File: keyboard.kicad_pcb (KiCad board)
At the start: 2 copper layers, 10 parts, among them U1 STM32F072CBT6

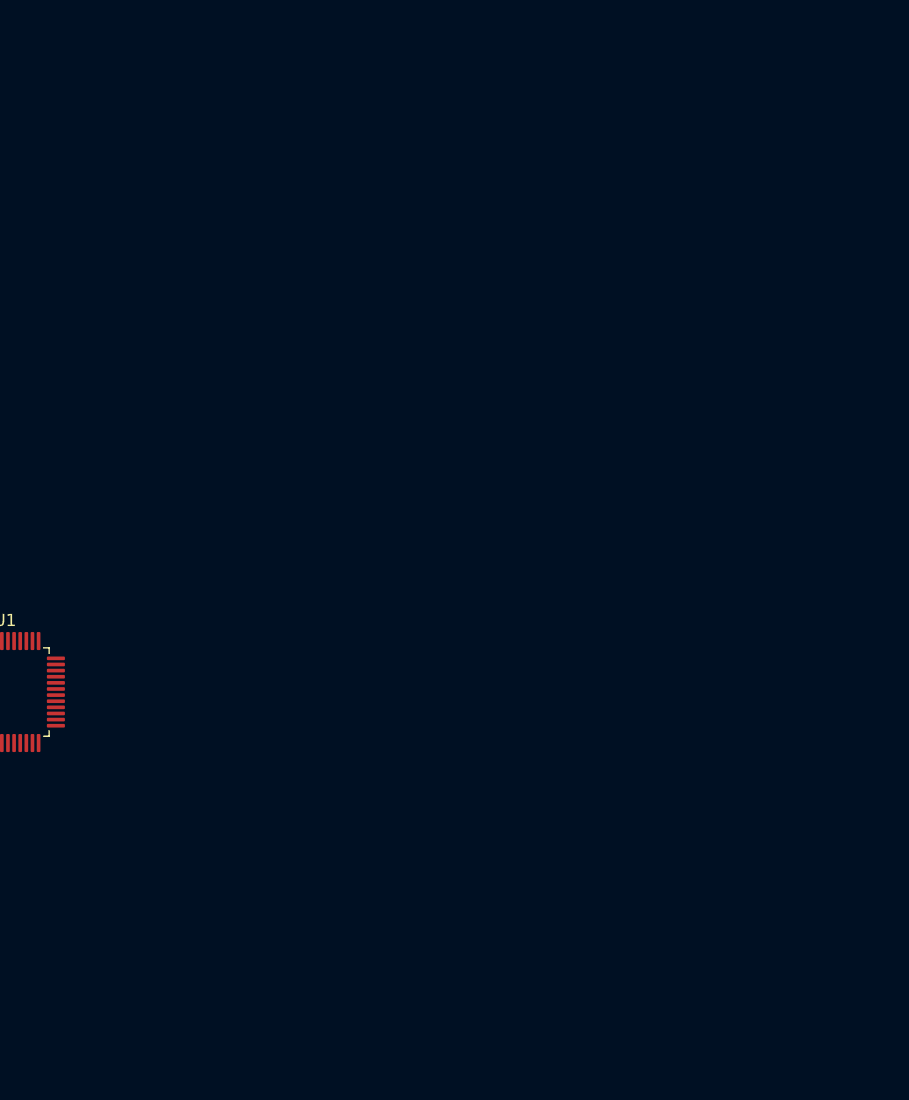
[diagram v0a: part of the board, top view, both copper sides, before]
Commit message: Added lcd display
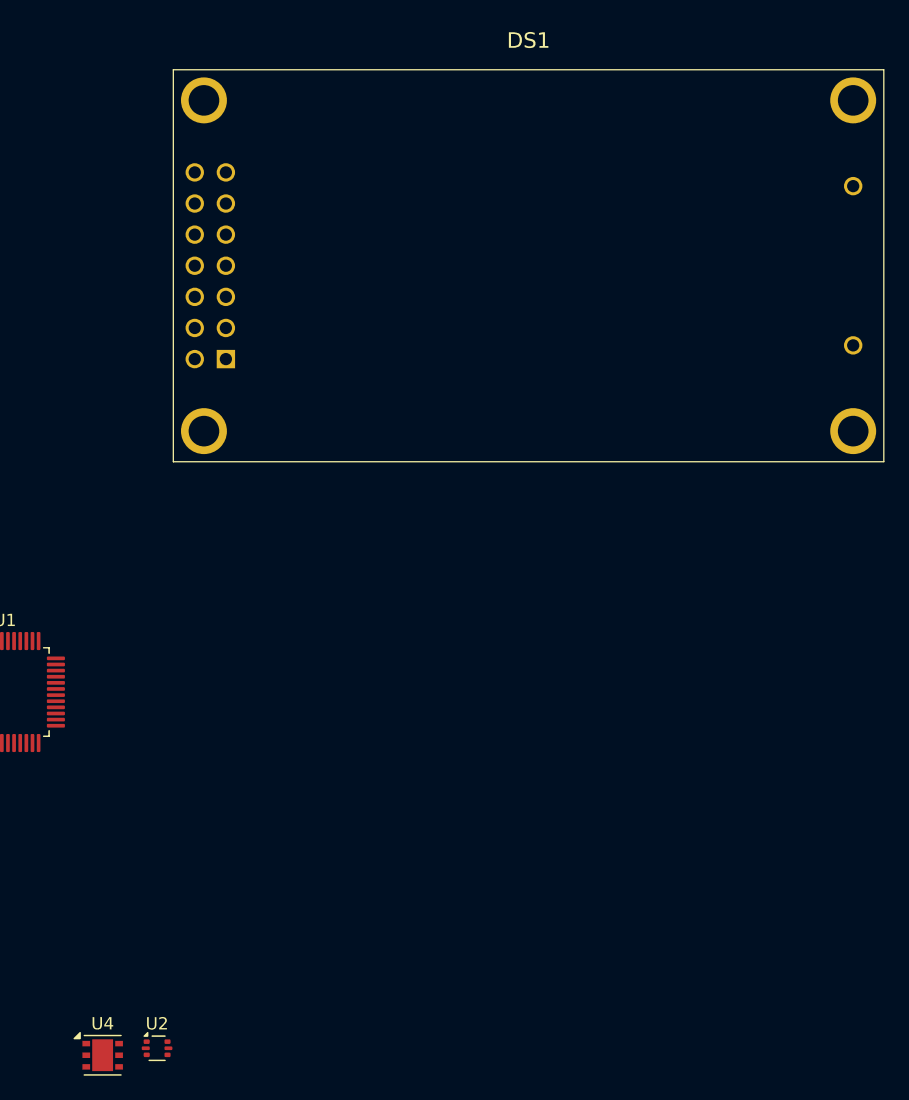
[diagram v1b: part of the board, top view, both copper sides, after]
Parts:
- added DS1: NHD-0208BZ-FL-YBW, NHD:NHD0208BZFLYBW, F.Cu at (118.8, 45.7)
- added U2: USBLC6-2P6, Package_TO_SOT_SMD:SOT-666, F.Cu at (113.2, 102.0)
- added U4: LDO40LPU33RY, Package_DFN_QFN:DFN-6-1EP_3x3mm_P0.95mm_EP1.7x2.6mm, F.Cu at (108.8, 102.5)
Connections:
- U1 pad 21: unconnected-(U1-PB10-Pad21) -> /LCD_ENABLE
- U1 pad 22: unconnected-(U1-PB11-Pad22) -> /DB4
- U1 pad 25: unconnected-(U1-PB12-Pad25) -> /DB5
- U1 pad 26: unconnected-(U1-PB13-Pad26) -> /DB6
- U1 pad 27: unconnected-(U1-PB14-Pad27) -> /DB7
- U1 pad 40: unconnected-(U1-PB4-Pad40) -> /OUT_A
- U1 pad 41: unconnected-(U1-PB5-Pad41) -> /OUT_B
- U1 pad 43: unconnected-(U1-PB7-Pad43) -> /MUTE
- U1 pad 45: unconnected-(U1-PB8-Pad45) -> /LED
- U1 pad 46: unconnected-(U1-PB9-Pad46) -> /LCD_RS

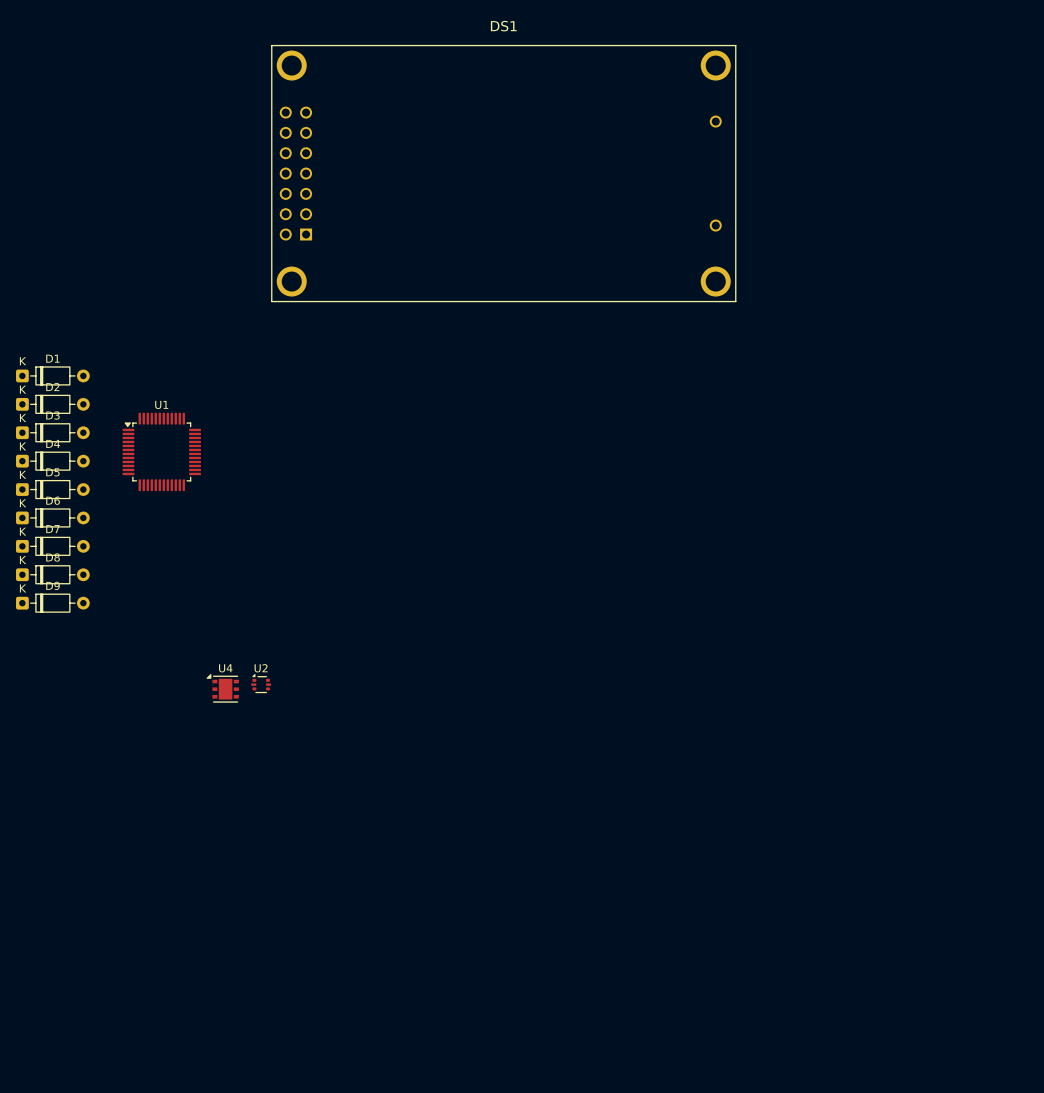
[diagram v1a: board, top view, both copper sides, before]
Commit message: Added key switches footprints
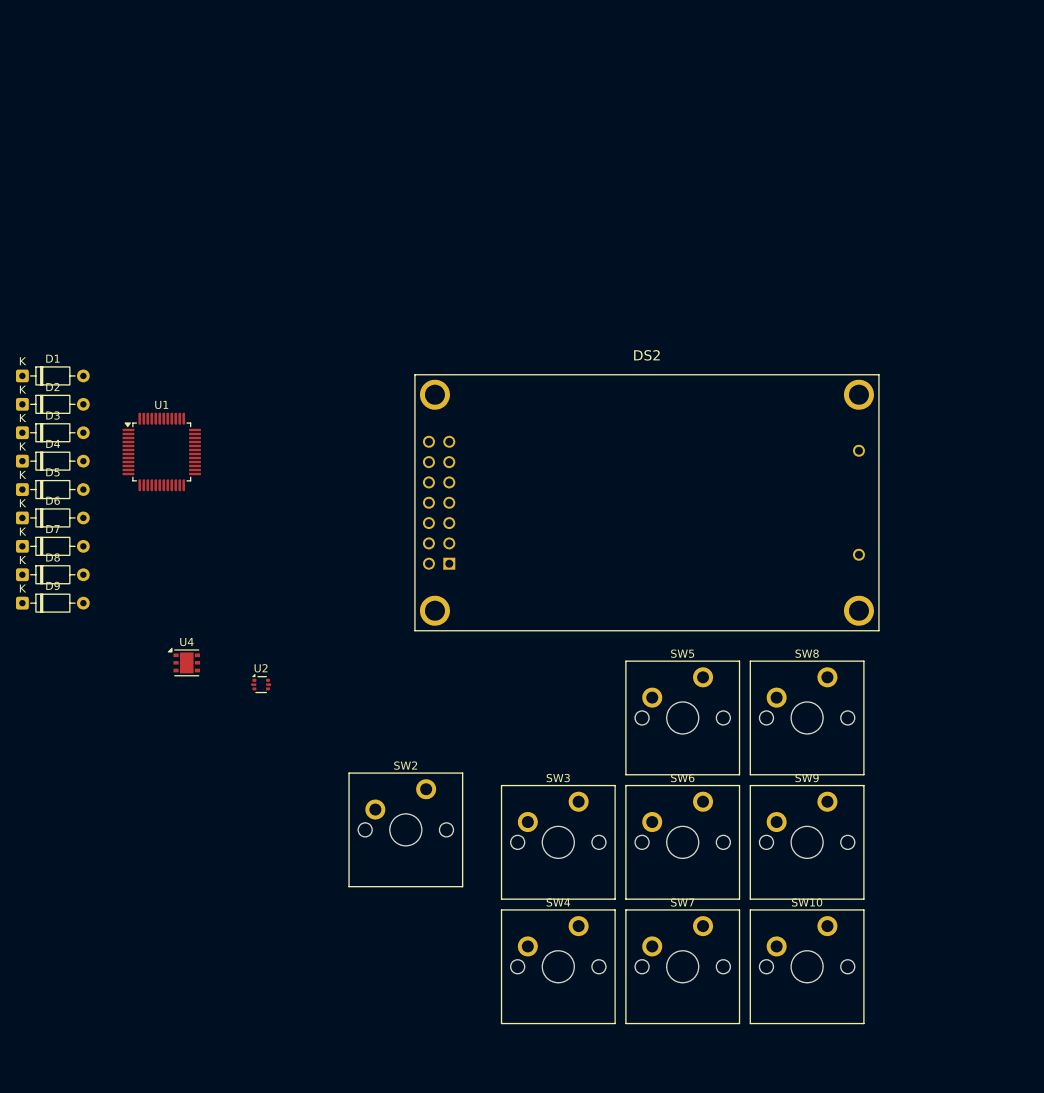
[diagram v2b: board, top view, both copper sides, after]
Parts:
- removed DS1: NHD-0208BZ-FL-YBW, NHD:NHD0208BZFLYBW
- added DS2: NHD-0208BZ-FL-YBW, NHD:NHD0208BZFLYBW, F.Cu at (136.7, 86.9)
- added SW10: SW_Push, Switch_Keyboard_Cherry_MX:SW_Cherry_MX_PCB_1.00u, F.Cu at (181.5, 137.2)
- added SW2: SW_Push, Switch_Keyboard_Cherry_MX:SW_Cherry_MX_PCB_1.00u, F.Cu at (131.3, 120.1)
- added SW3: SW_Push, Switch_Keyboard_Cherry_MX:SW_Cherry_MX_PCB_1.00u, F.Cu at (150.4, 121.7)
- added SW4: SW_Push, Switch_Keyboard_Cherry_MX:SW_Cherry_MX_PCB_1.00u, F.Cu at (150.4, 137.2)
- added SW5: SW_Push, Switch_Keyboard_Cherry_MX:SW_Cherry_MX_PCB_1.00u, F.Cu at (165.9, 106.2)
- added SW6: SW_Push, Switch_Keyboard_Cherry_MX:SW_Cherry_MX_PCB_1.00u, F.Cu at (165.9, 121.7)
- added SW7: SW_Push, Switch_Keyboard_Cherry_MX:SW_Cherry_MX_PCB_1.00u, F.Cu at (165.9, 137.2)
- added SW8: SW_Push, Switch_Keyboard_Cherry_MX:SW_Cherry_MX_PCB_1.00u, F.Cu at (181.5, 106.2)
- added SW9: SW_Push, Switch_Keyboard_Cherry_MX:SW_Cherry_MX_PCB_1.00u, F.Cu at (181.5, 121.7)
- moved U4 5.86 mm to (103.9, 99.3)

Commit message: Added footprints and placement
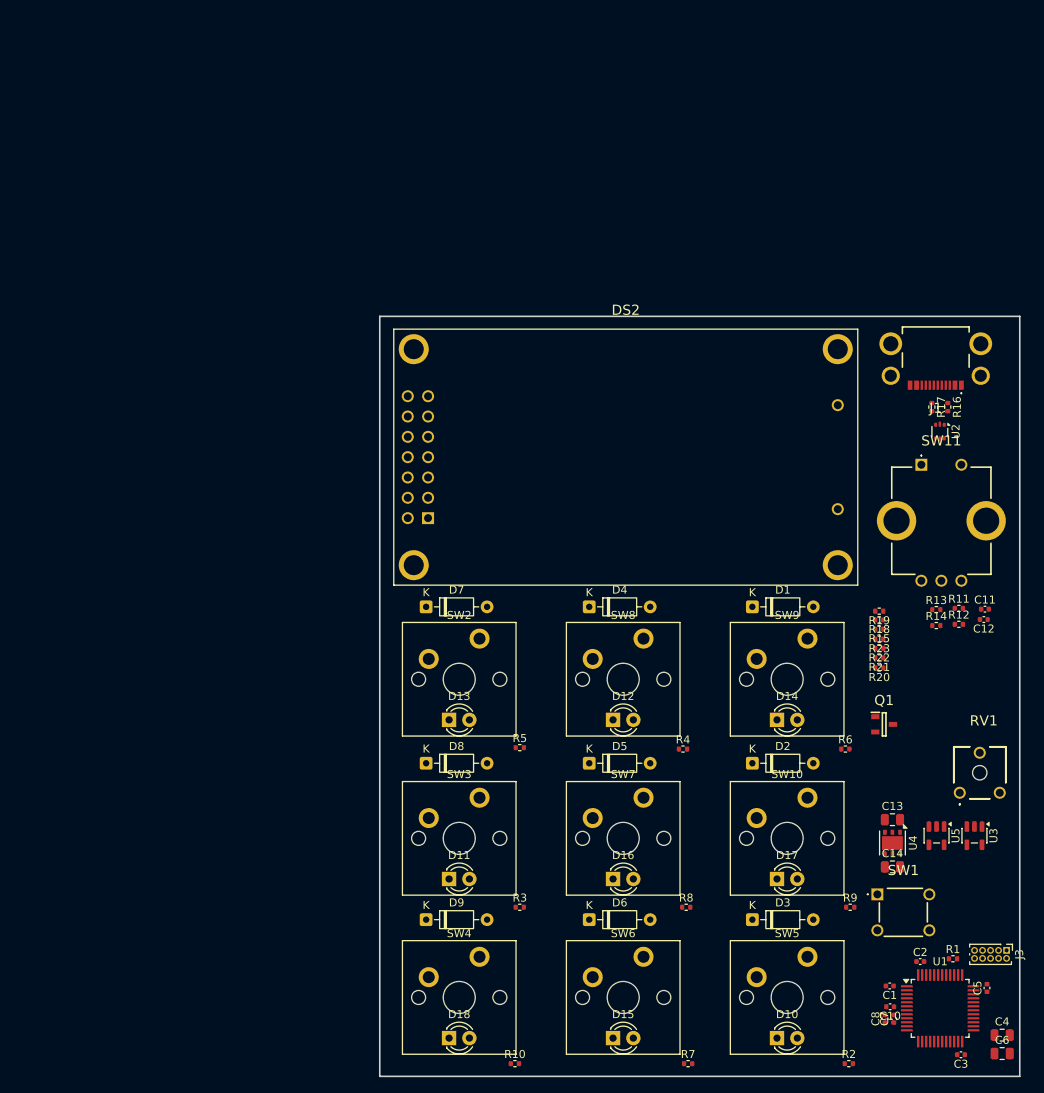
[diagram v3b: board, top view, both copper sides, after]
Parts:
- added C1: 100n, Capacitor_SMD:C_0402_1005Metric, F.Cu at (191.8, 139.7)
- added C10: 100n, Capacitor_SMD:C_0402_1005Metric, F.Cu at (191.8, 142.2)
- added C11: 100n, Capacitor_SMD:C_0402_1005Metric, F.Cu at (203.7, 92.5)
- added C12: 100n, Capacitor_SMD:C_0402_1005Metric, F.Cu at (203.6, 93.8)
- added C13: 4.7u, Capacitor_SMD:C_0805_2012Metric, F.Cu at (192.1, 118.9)
- added C14: 4.7u, Capacitor_SMD:C_0805_2012Metric, F.Cu at (192.1, 124.8)
- added C2: 100n, Capacitor_SMD:C_0402_1005Metric, F.Cu at (195.6, 136.6)
- added C3: 100n, Capacitor_SMD:C_0402_1005Metric, F.Cu at (200.7, 148.2)
- added C4: 4.7u, Capacitor_SMD:C_0805_2012Metric, F.Cu at (205.8, 145.8)
- added C5: 100n, Capacitor_SMD:C_0402_1005Metric, F.Cu at (203.9, 139.9)
- added C6: 4.7u, Capacitor_SMD:C_0805_2012Metric, F.Cu at (205.8, 148.1)
- added C7: 100n, Capacitor_SMD:C_0402_1005Metric, F.Cu at (192.3, 143.8)
- added C8: 1u, Capacitor_SMD:C_0402_1005Metric, F.Cu at (191.2, 143.8)
- added D10: LED, LED_THT:LED_D3.0mm, F.Cu at (177.7, 146.2)
- added D11: LED, LED_THT:LED_D3.0mm, F.Cu at (136.7, 126.3)
- added D12: LED, LED_THT:LED_D3.0mm, F.Cu at (157.2, 106.4)
- added D13: LED, LED_THT:LED_D3.0mm, F.Cu at (136.7, 106.4)
- added D14: LED, LED_THT:LED_D3.0mm, F.Cu at (177.7, 106.4)
- added D15: LED, LED_THT:LED_D3.0mm, F.Cu at (157.2, 146.2)
- added D16: LED, LED_THT:LED_D3.0mm, F.Cu at (157.2, 126.3)
- added D17: LED, LED_THT:LED_D3.0mm, F.Cu at (177.7, 126.3)
- added D18: LED, LED_THT:LED_D3.0mm, F.Cu at (136.7, 146.2)
- added J1: USB_C_Receptacle_USB2.0_16P, my_footprints:UJ20CHGMSMT4BP16TR, F.Cu at (197.6, 60.9)
- added J3: Conn_01x10_Pin, Connector_PinHeader_1.00mm:PinHeader_2x05_P1.00mm_Vertical, F.Cu at (206.4, 135.2)
- added Q1: NMOS, my_footprints:SOT95P230X110-3N, F.Cu at (191.1, 107.0)
- added R1: 10k, Resistor_SMD:R_0402_1005Metric, F.Cu at (199.7, 136.2)
- added R10: 330R, Resistor_SMD:R_0402_1005Metric, F.Cu at (144.9, 149.4)
- added R11: 10k, Resistor_SMD:R_0402_1005Metric, F.Cu at (200.4, 92.5)
- added R12: 10k, Resistor_SMD:R_0402_1005Metric, F.Cu at (200.4, 94.4)
- added R13: 10k, Resistor_SMD:R_0402_1005Metric, F.Cu at (197.6, 92.6)
- added R14: 10k, Resistor_SMD:R_0402_1005Metric, F.Cu at (197.6, 94.6)
- added R15: 330R, Resistor_SMD:R_0402_1005Metric, F.Cu at (190.5, 95.0)
- added R16: 5k1, Resistor_SMD:R_0402_1005Metric, F.Cu at (199.1, 67.3)
- added R17: 5k1, Resistor_SMD:R_0402_1005Metric, F.Cu at (197.1, 67.3)
- added R18: 330R, Resistor_SMD:R_0402_1005Metric, F.Cu at (190.5, 93.9)
- added R19: 330R, Resistor_SMD:R_0402_1005Metric, F.Cu at (190.5, 92.8)
- added R2: 330R, Resistor_SMD:R_0402_1005Metric, F.Cu at (186.7, 149.4)
- added R20: 330R, Resistor_SMD:R_0402_1005Metric, F.Cu at (190.5, 99.9)
- added R21: 330R, Resistor_SMD:R_0402_1005Metric, F.Cu at (190.5, 98.6)
- added R22: 330R, Resistor_SMD:R_0402_1005Metric, F.Cu at (190.5, 97.5)
- added R23: 330R, Resistor_SMD:R_0402_1005Metric, F.Cu at (190.5, 96.3)
- added R3: 330R, Resistor_SMD:R_0402_1005Metric, F.Cu at (145.6, 129.8)
- added R4: 330R, Resistor_SMD:R_0402_1005Metric, F.Cu at (166.0, 110.0)
- added R5: 330R, Resistor_SMD:R_0402_1005Metric, F.Cu at (145.6, 109.9)
- added R6: 330R, Resistor_SMD:R_0402_1005Metric, F.Cu at (186.3, 110.0)
- added R7: 330R, Resistor_SMD:R_0402_1005Metric, F.Cu at (166.6, 149.4)
- added R8: 330R, Resistor_SMD:R_0402_1005Metric, F.Cu at (166.4, 129.8)
- added R9: 330R, Resistor_SMD:R_0402_1005Metric, F.Cu at (186.9, 129.8)
- added RV1: 10k, my_footprints:601030, F.Cu at (200.6, 115.5)
- added SW1: SW_Push, my_footprints:TS0266100BK100LCRD, F.Cu at (190.2, 128.2)
- added SW11: RotaryEncoder_Switch, my_footprints:PEC12R3220FS0024, F.Cu at (195.8, 74.5)
- added U3: SN74LV1T34DBV, Package_TO_SOT_SMD:SOT-23-5, F.Cu at (202.4, 120.9)
- added U5: SN74LV1T34DBV, Package_TO_SOT_SMD:SOT-23-5, F.Cu at (197.7, 120.9)
- moved U1 119.6 mm to (198.1, 142.4)
- moved D3 109.7 mm to (174.6, 131.4)
- moved D2 101.7 mm to (174.6, 111.8)
- moved D1 95.7 mm to (174.6, 92.3)
- moved U4 91.0 mm to (192.1, 121.8), turned to -90 degrees
- moved U2 90.5 mm to (198.1, 70.3), turned to -90 degrees
- moved D6 86.8 mm to (154.2, 131.4)
- moved D5 78.7 mm to (154.2, 111.8)
- moved D4 73.2 mm to (154.2, 92.3)
- moved D9 64.1 mm to (133.8, 131.4)
- moved D8 55.7 mm to (133.8, 111.8)
- moved D7 51.0 mm to (133.8, 92.3)
- moved SW5 37.3 mm to (179.0, 141.1)
- moved SW8 23.5 mm to (158.5, 101.3)
- moved SW6 20.8 mm to (158.5, 141.1)
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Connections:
- U1 pad 9: +3.3VA -> +3.3V
- U4 pad 2: Net-(D20-K) -> +5V
- U4 pad 3: Net-(D20-K) -> +5V
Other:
- board outline added: 80 x 95 mm

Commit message: Added pcb routing
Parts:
- removed U2: USBLC6-2P6, Package_TO_SOT_SMD:SOT-666
- added U6: USBLC6-2SC6, Package_TO_SOT_SMD:SOT-23-6, F.Cu at (189.4, 54.8)
- J1: footprint my_footprints:UJ20CHGMSMT4BP16TR -> Connector_USB:USB_C_Receptacle_GCT_USB4105-xx-A_16P_TopMnt_Horizontal
- moved RV1 43.2 mm to (187.0, 74.5), turned to 90 degrees
- moved R20 34.7 mm to (181.5, 66.3)
- moved R18 34.7 mm to (181.5, 60.4)
- moved R22 34.7 mm to (181.5, 63.9)
- moved R15 34.7 mm to (181.5, 61.5)
- moved R19 34.7 mm to (181.5, 59.2)
- moved R21 34.7 mm to (181.5, 65.1)
- moved R23 34.7 mm to (181.5, 62.8)
- moved R16 26.4 mm to (182.2, 47.0), turned to 90 degrees
- moved C12 20.6 mm to (186.8, 105.8), turned to 0 degrees
- moved R17 20.3 mm to (195.9, 47.0), turned to 90 degrees
- moved R1 17.7 mm to (188.6, 122.4)
- moved R11 17.7 mm to (186.8, 103.7)
- moved J1 17.0 mm to (189.1, 46.1)
- moved J3 16.2 mm to (196.7, 122.3)
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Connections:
- C14 pad 1: +3V3 -> +3.3V
- J3 pad 2: /SWCLK -> /SWDIO
- J3 pad 4: /SWDIO -> /SWCLK
- U1 pad 11: unconnected-(U1-PA1-Pad11) -> /LCD_RS
- U1 pad 12: unconnected-(U1-PA2-Pad12) -> /LCD_ENABLE
- U1 pad 13: unconnected-(U1-PA3-Pad13) -> Row 1
- U1 pad 14: unconnected-(U1-PA4-Pad14) -> Row 2
- U1 pad 15: Column 3 -> Row 3
- U1 pad 16: Column 2 -> unconnected-(U1-PA6-Pad16)
- U1 pad 17: Column 1 -> unconnected-(U1-PA7-Pad17)
- U1 pad 2: unconnected-(U1-PC13-Pad2) -> Column 1
- U1 pad 21: /LCD_ENABLE -> unconnected-(U1-PB10-Pad21)
- U1 pad 22: /DB4 -> unconnected-(U1-PB11-Pad22)
- U1 pad 25: /DB5 -> /DB4
- U1 pad 26: /DB6 -> /DB5
- U1 pad 27: /DB7 -> /DB6
- U1 pad 28: unconnected-(U1-PB15-Pad28) -> /DB7
- U1 pad 29: Row 3 -> unconnected-(U1-PA8-Pad29)
- U1 pad 3: unconnected-(U1-PC14-Pad3) -> Column 2
- U1 pad 30: Row 2 -> unconnected-(U1-PA9-Pad30)
- U1 pad 31: Row 1 -> unconnected-(U1-PA10-Pad31)
- U1 pad 39: unconnected-(U1-PB3-Pad39) -> /MUTE
- U1 pad 4: unconnected-(U1-PC15-Pad4) -> Column 3
- U1 pad 40: /OUT_A -> /OUT_B
- U1 pad 41: /OUT_B -> /OUT_A
- U1 pad 43: /MUTE -> unconnected-(U1-PB7-Pad43)
- U1 pad 46: /LCD_RS -> unconnected-(U1-PB9-Pad46)
- U3 pad 5: +3V3 -> +3.3V
- U4 pad 4: +3V3 -> +3.3V
- U4 pad 5: +3V3 -> +3.3V
- U5 pad 5: +3V3 -> +3.3V
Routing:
- net Net-(D10-K): track 0.00 -> 195.9 mm
- net /DB4: track 0.00 -> 158.2 mm
- net /DB5: track 0.00 -> 141.7 mm, vias 0 -> 1
- net /DB6: track 0.00 -> 140.3 mm, vias 0 -> 1
- net /LCD_ENABLE: track 0.00 -> 137.1 mm
- net /LCD_RS: track 0.00 -> 134.0 mm
- net /DB7: track 0.00 -> 131.6 mm, vias 0 -> 1
- net Row 1: track 0.00 -> 113.7 mm, vias 0 -> 1
- net Row 2: track 0.00 -> 96.9 mm, vias 0 -> 1
- net Column 1: track 0.00 -> 95.4 mm
- net /USB_D-: track 0.00 -> 83.2 mm
- net /USB_D+: track 0.00 -> 82.5 mm
- net Row 3: track 0.00 -> 75.0 mm, vias 0 -> 1
- net Column 2: track 0.00 -> 74.2 mm
- net Column 3: track 0.00 -> 60.9 mm
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- added copper zone on B.Cu, net +3.3V
- added copper zone on F.Cu, net +3.3V
- added copper zone on B.Cu, net +5V
- added copper zone on F.Cu, net +5V
- added copper zone on F.Cu, net GND
- added copper zone on In1.Cu, net GND
- added copper zone on In2.Cu, net GND
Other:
- board size 80 x 95 mm -> 82 x 96 mm
- copper layers 2 -> 4
